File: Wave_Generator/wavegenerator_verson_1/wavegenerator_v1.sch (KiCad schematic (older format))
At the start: 56 parts, among them J1 01x06, J2 USB_B_Micro, J3 Conn_Coaxial, J6 1x2Pinheader, SW1 button, SW2 button, SW3 SP3T, U1 ATmega328P-AU, U3 LinReg, U4 MAX038CPP, U5 MC33063AD, U7 LM318N, Y1 16MHz

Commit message: OP AMP ERRORS
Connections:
- net GND: no longer U7.1 (BAL1), U7.5 (BAL3), U7.8 (BAL2)
- no-connect marks 3 -> 6
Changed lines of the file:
@@
 	0    -1   -1   0
-$EndComp
-$Comp
-L power:GND #PWR0103
-U 1 1 5D8C0155
-P 5500 1150
-F 0 "#PWR0103" H 5500 900 50  0001 C CNN
-F 1 "GND" H 5505 977 50  0000 C CNN
-F 2 "" H 5500 1150 50  0001 C CNN
-F 3 "" H 5500 1150 50  0001 C CNN
-	1    5500 1150
-	1    0    0    -1
 $EndComp
 Wire Wire Line
@@
 	-1   0    0    1
 $EndComp
-$Comp
-L power:GND #PWR0105
-U 1 1 5D8F5A55
-P 5450 1750
-F 0 "#PWR0105" H 5450 1500 50  0001 C CNN
-F 1 "GND" H 5550 1800 50  0000 C CNN
-F 2 "" H 5450 1750 50  0001 C CNN
-F 3 "" H 5450 1750 50  0001 C CNN
-	1    5450 1750
-	1    0    0    -1
-$EndComp
-Wire Wire Line
-	5350 1750 5450 1750
-Connection ~ 5450 1750
 Wire Wire Line
 	5650 1450 5650 1900
-Wire Wire Line
-	5350 1150 5500 1150
 Wire Wire Line
 	4350 1100 4350 1200
@@
 Wire Wire Line
 	1850 1200 2950 1200
+NoConn ~ 5350 1750
+NoConn ~ 5450 1750
+NoConn ~ 5350 1150
 $EndSCHEMATC

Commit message: wavegenerator changes
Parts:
- added TP5: WS_0, TestPoint:TestPoint_THTPad_2.5x2.5mm_Drill1.2mm, symbol Connector:TestPoint
- added TP6: WS_1, TestPoint:TestPoint_THTPad_2.5x2.5mm_Drill1.2mm, symbol Connector:TestPoint
- added TP7: Sync, TestPoint:TestPoint_THTPad_2.5x2.5mm_Drill1.2mm, symbol Connector:TestPoint
- added TP8: output, TestPoint:TestPoint_THTPad_2.5x2.5mm_Drill1.2mm, symbol Connector:TestPoint
- C4: renamed from C16; footprint Capacitor_THT:C_Disc_D3.0mm_W1.6mm_P2.50mm -> Capacitor_THT:C_Rect_L4.0mm_W2.5mm_P2.50mm
- C5: renamed from C17; footprint Capacitor_THT:C_Disc_D3.0mm_W1.6mm_P2.50mm -> Capacitor_THT:C_Rect_L4.0mm_W2.5mm_P2.50mm
- H1, H2, H3, H4: footprint MountingHole:MountingHole_2.1mm -> MountingHole:MountingHole_3.2mm_M3
- J1: value 01x06 -> 01x05; footprint wavegenerator_v1:01x06_pin_header -> wavegenerator_v1:01x05_pin_header
- R6: renamed from R11; value 1k -> 10k
- renumbered C13 to C1, C18 to C10, C1 to C101, C2 to C102, C14 to C103, C3 to C104, C4 to C105, C8 to C106, C11 to C107, C10 to C11, C15 to C2, C12 to C3, C5 to C6, C6 to C7, C7 to C8, R6 to R1, R8 to R101, R9 to R102, R10 to R103, R1 to R104, R5 to R2, R2 to R3, R3 to R4, R4 to R5, R12 to R7
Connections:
- net GND: now also J1.5
- net WS_0: now also TP5.1
- net WS_1: now also TP6.1
- net reset: now also J1.4, R104.2, SW2.1, U1.29 (~RESET~/PC6); no longer MOD1.5 (RES), U1.28 (PC5)
- net sync: now also U1.12 (PB0), TP7.1
- net switch_n: now reaches SW1.1, U1.2 (PD4)
- net MISO: now reaches J1.1, U1.16 (PB4)
- net output: now reaches RV3.3
- net output: now also TP8.1
- new net reset_lcd: MOD1.5 (RES), U1.28 (PC5)
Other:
- moved on the sheet: R104, SW1, SW2, TP1, TP2, TP3, TP4

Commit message: touch ups
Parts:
- added R8: 10k, Resistor_THT:R_Axial_DIN0207_L6.3mm_D2.5mm_P10.16mm_Horizontal, symbol Device:R_Small_US
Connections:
- net GND: now also U4.12 (PDO)
- net at U7.3 (+): now also R8.1; no longer RV3.2
- new net: R8.2, RV3.2
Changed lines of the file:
@@
 U 1 1 5D1B4472
 P 2500 5900
-F 0 "R103" H 2550 5950 50  0000 L CNN
-F 1 "10k" H 2550 5850 50  0000 L CNN
+F 0 "R103" H 2250 5950 50  0000 L CNN
+F 1 "10k" H 2300 5850 50  0000 L CNN
 F 2 "Resistor_SMD:R_0805_2012Metric" H 2500 5900 50  0001 C CNN
 F 3 "~" H 2500 5900 50  0001 C CNN
@@
 P 1500 6000
 F 0 "#PWR035" H 1500 5750 50  0001 C CNN
-F 1 "GND" H 1505 5827 50  0000 C CNN
+F 1 "GND" H 1500 5850 50  0000 C CNN
 F 2 "" H 1500 6000 50  0001 C CNN
 F 3 "" H 1500 6000 50  0001 C CNN
@@
 P 2500 6000
 F 0 "#PWR047" H 2500 5750 50  0001 C CNN
-F 1 "GND" H 2505 5827 50  0000 C CNN
+F 1 "GND" H 2500 5850 50  0000 C CNN
 F 2 "" H 2500 6000 50  0001 C CNN
 F 3 "" H 2500 6000 50  0001 C CNN
@@
 $EndComp
 Wire Wire Line
-	1050 5800 1350 5800
-Wire Wire Line
-	2700 5700 2700 6150
-Connection ~ 1350 5800
-Wire Wire Line
-	1350 5800 1500 5800
+	1050 5800 1150 5800
 Wire Wire Line
 	1250 4550 1250 4900
@@
 U 1 1 5D65F834
 P 4350 1350
-F 0 "RV3" H 4600 1550 50  0000 C CNN
-F 1 "10k" H 4600 1450 50  0000 C CNN
+F 0 "RV3" H 4500 1450 50  0000 C CNN
+F 1 "10k" H 4500 1550 50  0000 C CNN
 F 2 "wavegenerator_v1:Potentiometer_PTV09A" H 4350 1350 50  0001 C CNN
 F 3 "~" H 4350 1350 50  0001 C CNN
@@
 L power:-5V #PWR034
 U 1 1 5D4EAB46
-P 1350 6150
-F 0 "#PWR034" H 1350 6250 50  0001 C CNN
-F 1 "-5V" H 1365 6323 50  0000 C CNN
-F 2 "" H 1350 6150 50  0001 C CNN
-F 3 "" H 1350 6150 50  0001 C CNN
-	1    1350 6150
+P 1150 6200
+F 0 "#PWR034" H 1150 6300 50  0001 C CNN
+F 1 "-5V" H 1165 6373 50  0000 C CNN
+F 2 "" H 1150 6200 50  0001 C CNN
+F 3 "" H 1150 6200 50  0001 C CNN
+	1    1150 6200
 	-1   0    0    1
 $EndComp
-Connection ~ 1350 6150
 $Comp
 L power:GND #PWR08
@@
 L power:GND #PWR029
 U 1 1 5D370EFF
-P 2500 3300
-F 0 "#PWR029" H 2500 3050 50  0001 C CNN
-F 1 "GND" H 2505 3127 50  0000 C CNN
-F 2 "" H 2500 3300 50  0001 C CNN
-F 3 "" H 2500 3300 50  0001 C CNN
-	1    2500 3300
+P 2500 3250
+F 0 "#PWR029" H 2500 3000 50  0001 C CNN
+F 1 "GND" H 2505 3077 50  0000 C CNN
+F 2 "" H 2500 3250 50  0001 C CNN
+F 3 "" H 2500 3250 50  0001 C CNN
+	1    2500 3250
 	1    0    0    -1
 $EndComp
@@
 	1    0    0    -1
 $EndComp
-Wire Wire Line
-	1350 6150 1350 5800
 $Comp
 L Connector:TestPoint TP4
@@
 	1    0    0    -1
 $EndComp
-Wire Wire Line
-	1350 6150 2700 6150
 $Comp
 L power:-5V #PWR0108
@@
 	3100 5300 3100 5500
 Connection ~ 2700 5300
-Wire Wire Line
-	4500 1350 5050 1350
 $Comp
 L Connector:Conn_Coaxial J3
@@
 Text Label 9200 1100 0    50   ~ 0
 sync
+Connection ~ 1150 5800
+Wire Wire Line
+	1150 5800 1500 5800
+Wire Wire Line
+	2700 6200 1150 6200
+Wire Wire Line
+	2700 5700 2700 6200
+Wire Wire Line
+	1150 5800 1150 6200
+Connection ~ 1150 6200
+$Comp
+L Device:R_Small_US R8
+U 1 1 5D3AF030
+P 4750 1350
+F 0 "R8" V 4850 1400 50  0000 C CNN
+F 1 "10k" V 4950 1400 50  0000 C CNN
+F 2 "Resistor_THT:R_Axial_DIN0207_L6.3mm_D2.5mm_P10.16mm_Horizontal" H 4750 1350 50  0001 C CNN
+F 3 "~" H 4750 1350 50  0001 C CNN
+	1    4750 1350
+	0    1    1    0
+$EndComp
+Wire Wire Line
+	4500 1350 4650 1350
+Wire Wire Line
+	4850 1350 5050 1350
 $EndSCHEMATC

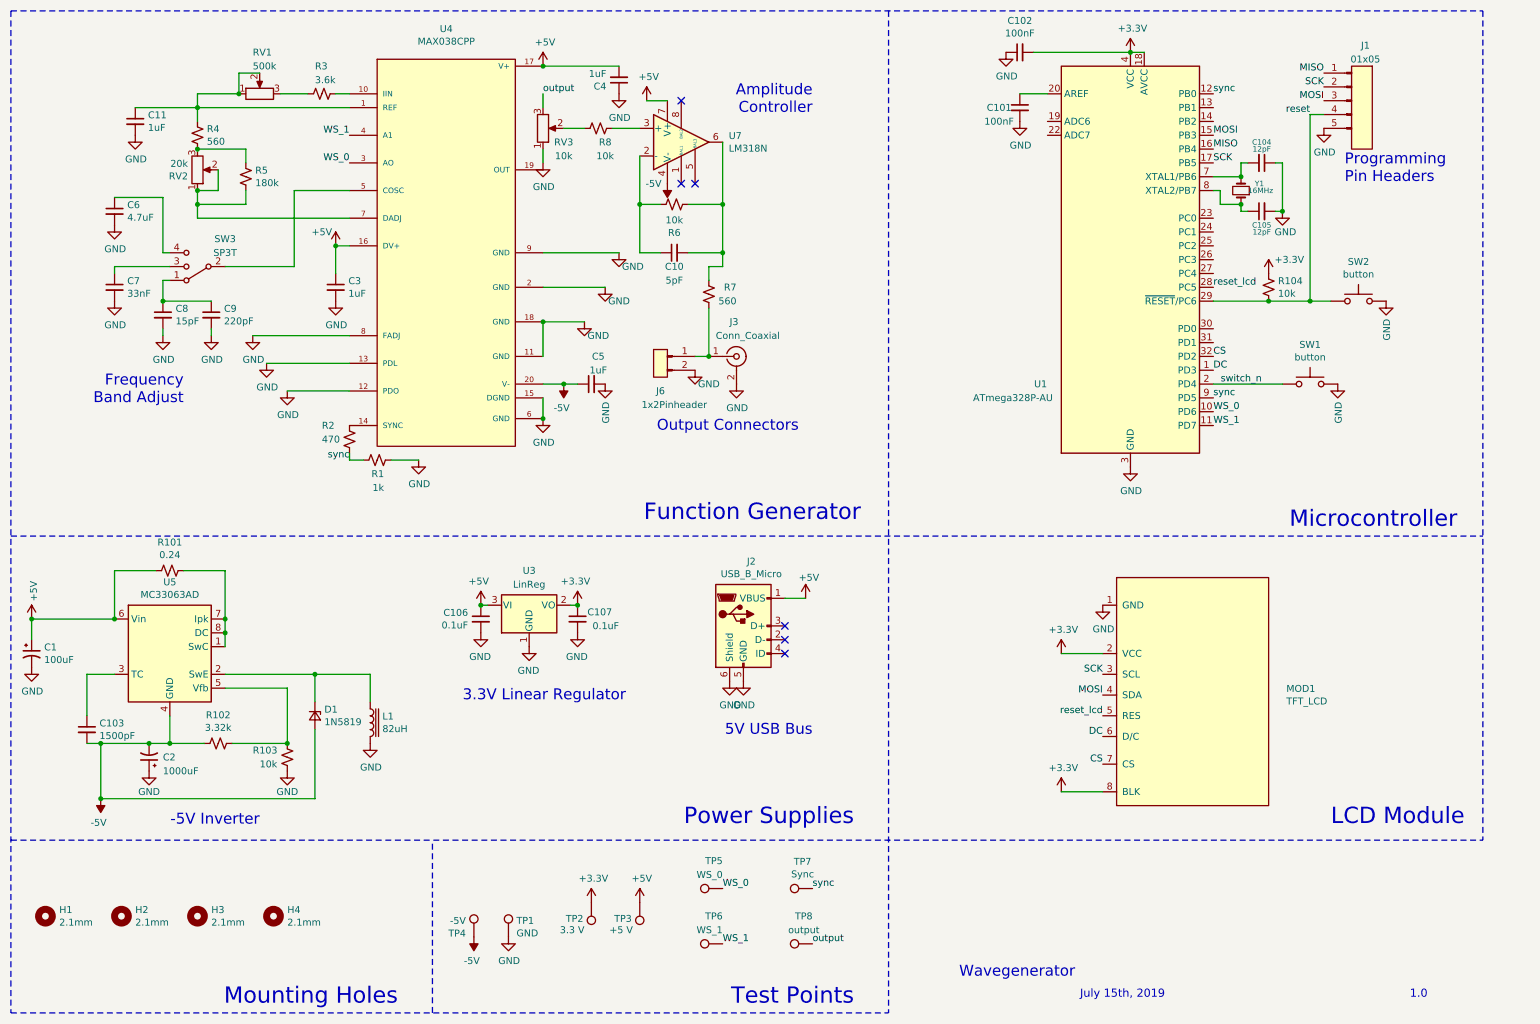
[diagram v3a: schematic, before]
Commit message: removed op amp and sync connection
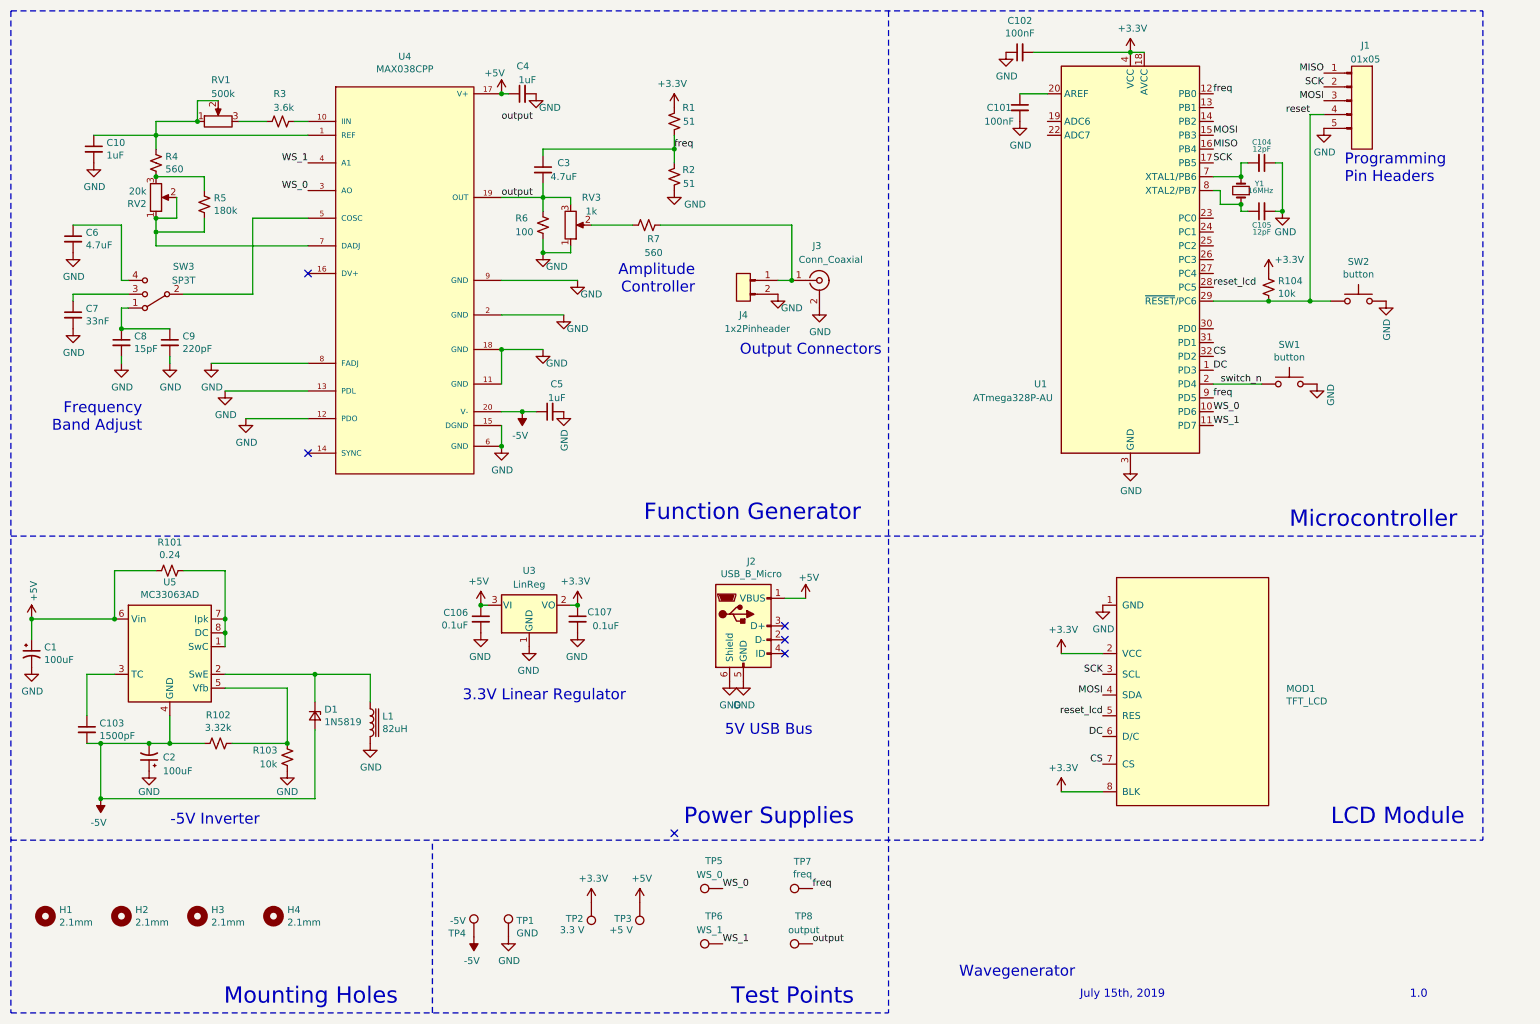
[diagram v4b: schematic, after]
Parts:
- removed C10: 5pF, Capacitor_THT:C_Rect_L4.0mm_W2.5mm_P2.50mm, symbol Device:C_Small
- removed R7: 560, Resistor_THT:R_Axial_DIN0207_L6.3mm_D2.5mm_P10.16mm_Horizontal, symbol Device:R_Small_US
- removed U7: LM318N, wavegenerator_v1:LM318N, symbol Amplifier_Operational:LM318N
- C2: value 1000uF -> 100uF
- C3: value 1uF -> 4.7uF
- R1: value 1k -> 51
- R2: value 470 -> 51
- R6: value 10k -> 100
- R7: renamed from R8; value 10k -> 560
- RV3: value 10k -> 1k
- TP7: value Sync -> freq
- renumbered C11 to C10, J6 to J4
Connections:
- net +3V3: now also R1.1
- net +5V: now also C4.1; no longer C3.1, C4.2, U4.16 (DV+)
- net GND: now also C4.2, R2.2, R6.2; no longer C3.2, C4.1, R1.2
- net output: now also C3.2, R6.1, U4.19 (OUT)
- net at U4.14 (SYNC): no longer R2.1
- net at R7.1: now also J3.1 (In), J4.1
- net sync renamed freq
- net freq: now also C3.1, R1.2, R2.1; no longer R1.1, R2.2
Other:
- moved on the sheet: C10, C4, C5, C6, C7, C8, C9, J3, J4, R3, R4, R5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

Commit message: naming
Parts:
- renumbered U3 to U1, U1 to U2, U5 to U3
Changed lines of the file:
@@
 	2050 5000 2050 5100
 $Comp
-L Regulator_Switching:MC33063AD U5
+L Regulator_Switching:MC33063AD U3
 U 1 1 5D1E6E42
 P 1650 5100
-F 0 "U5" H 1650 5567 50  0000 C CNN
+F 0 "U3" H 1650 5567 50  0000 C CNN
 F 1 "MC33063AD" H 1650 5476 50  0000 C CNN
 F 2 "Package_SO:SOIC-8_3.9x4.9mm_P1.27mm" H 1700 4650 50  0001 L CNN
@@
 	6100 4750 6250 4750
 $Comp
-L MCU_Microchip_ATmega:ATmega328P-AU U1
+L MCU_Microchip_ATmega:ATmega328P-AU U2
 U 1 1 5D258DD6
 P 8600 2300
-F 0 "U1" H 7950 1400 50  0000 C CNN
+F 0 "U2" H 7950 1400 50  0000 C CNN
 F 1 "ATmega328P-AU" H 7750 1300 50  0000 C CNN
 F 2 "Package_QFP:TQFP-32_7x7mm_P0.8mm" H 8600 2300 50  0001 C CIN
@@
 $EndComp
 $Comp
-L Regulator_Linear:AP1117-33 U3
+L Regulator_Linear:AP1117-33 U1
 U 1 1 5D2563E2
 P 4250 4800
-F 0 "U3" H 4250 5050 50  0000 C CNN
+F 0 "U1" H 4250 5050 50  0000 C CNN
 F 1 "LinReg" H 4250 4950 50  0000 C CNN
 F 2 "Package_TO_SOT_SMD:SOT-223-3_TabPin2" H 4250 4600 50  0001 C CIN

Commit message: numbering
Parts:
- added C5, C7: 10nF, Capacitor_THT:C_Rect_L4.0mm_W2.5mm_P2.50mm, symbol Device:C_Small
- renumbered C8 to C10, C9 to C11, C10 to C12, C5 to C6, C6 to C8, C7 to C9
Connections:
- net +5V: now also C5.2
- net -5V: now also C7.2
- net GND: now also C5.1, C7.1
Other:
- moved on the sheet: C6
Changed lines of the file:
@@
 $EndComp
 $Comp
-L Device:C_Small C8
+L Device:C_Small C10
 U 1 1 5D379378
 P 1300 2900
-F 0 "C8" H 1392 2946 50  0000 L CNN
+F 0 "C10" H 1392 2946 50  0000 L CNN
 F 1 "15pF" H 1392 2855 50  0000 L CNN
 F 2 "Capacitor_THT:C_Rect_L4.0mm_W2.5mm_P2.50mm" H 1300 2900 50  0001 C CNN
@@
 	1350 2650 1300 2650
 $Comp
-L Device:C_Small C6
+L Device:C_Small C8
 U 1 1 5D37A6B1
 P 950 2150
-F 0 "C6" H 1042 2196 50  0000 L CNN
+F 0 "C8" H 1042 2196 50  0000 L CNN
 F 1 "4.7uF" H 1042 2105 50  0000 L CNN
 F 2 "Capacitor_THT:C_Rect_L4.0mm_W2.5mm_P2.50mm" H 950 2150 50  0001 C CNN
@@
 $EndComp
 $Comp
-L Device:C_Small C7
+L Device:C_Small C9
 U 1 1 5D379EFA
 P 950 2700
-F 0 "C7" H 1042 2746 50  0000 L CNN
+F 0 "C9" H 1042 2746 50  0000 L CNN
 F 1 "33nF" H 1042 2655 50  0000 L CNN
 F 2 "Capacitor_THT:C_Rect_L4.0mm_W2.5mm_P2.50mm" H 950 2700 50  0001 C CNN
@@
 $EndComp
 $Comp
-L Device:C_Small C10
+L Device:C_Small C12
 U 1 1 5D2356A9
 P 1100 1500
-F 0 "C10" H 1192 1546 50  0000 L CNN
+F 0 "C12" H 1192 1546 50  0000 L CNN
 F 1 "1uF" H 1192 1455 50  0000 L CNN
 F 2 "Capacitor_THT:C_Rect_L4.0mm_W2.5mm_P2.50mm" H 1100 1500 50  0001 C CNN
@@
 $EndComp
 $Comp
-L Device:C_Small C5
+L Device:C_Small C6
 U 1 1 5D248DFE
-P 4400 3400
-F 0 "C5" V 4600 3350 50  0000 C CNN
-F 1 "1uF" V 4500 3350 50  0000 C CNN
-F 2 "Capacitor_THT:C_Rect_L4.0mm_W2.5mm_P2.50mm" H 4400 3400 50  0001 C CNN
-F 3 "~" H 4400 3400 50  0001 C CNN
-	1    4400 3400
+P 4450 3400
+F 0 "C6" V 4650 3400 50  0000 C CNN
+F 1 "1uF" V 4550 3400 50  0000 C CNN
+F 2 "Capacitor_THT:C_Rect_L4.0mm_W2.5mm_P2.50mm" H 4450 3400 50  0001 C CNN
+F 3 "~" H 4450 3400 50  0001 C CNN
+	1    4450 3400
 	0    -1   -1   0
 $EndComp
@@
 L power:GND #PWR045
 U 1 1 5D24B84C
-P 4500 3400
-F 0 "#PWR045" H 4500 3150 50  0001 C CNN
-F 1 "GND" V 4505 3272 50  0000 R CNN
-F 2 "" H 4500 3400 50  0001 C CNN
-F 3 "" H 4500 3400 50  0001 C CNN
-	1    4500 3400
+P 4650 3600
+F 0 "#PWR045" H 4650 3350 50  0001 C CNN
+F 1 "GND" H 4850 3500 50  0000 R CNN
+F 2 "" H 4650 3600 50  0001 C CNN
+F 3 "" H 4650 3600 50  0001 C CNN
+	1    4650 3600
 	1    0    0    -1
 $EndComp
@@
 	-1   0    0    1
 $EndComp
-Wire Wire Line
-	4200 3400 4300 3400
 $Comp
 L power:-5V #PWR034
@@
 L power:GND #PWR042
 U 1 1 5D298258
-P 4300 1100
-F 0 "#PWR042" H 4300 850 50  0001 C CNN
-F 1 "GND" H 4400 1000 50  0000 C CNN
-F 2 "" H 4300 1100 50  0001 C CNN
-F 3 "" H 4300 1100 50  0001 C CNN
-	1    4300 1100
+P 4400 1350
+F 0 "#PWR042" H 4400 1100 50  0001 C CNN
+F 1 "GND" H 4500 1250 50  0000 C CNN
+F 2 "" H 4400 1350 50  0001 C CNN
+F 3 "" H 4400 1350 50  0001 C CNN
+	1    4400 1350
 	1    0    0    -1
 $EndComp
@@
 $EndComp
 $Comp
-L Device:C_Small C9
+L Device:C_Small C11
 U 1 1 5D573068
 P 1650 2900
-F 0 "C9" H 1742 2946 50  0000 L CNN
+F 0 "C11" H 1742 2946 50  0000 L CNN
 F 1 "220pF" H 1742 2855 50  0000 L CNN
 F 2 "Capacitor_THT:C_Rect_L4.0mm_W2.5mm_P2.50mm" H 1650 2900 50  0001 C CNN
@@
 Text Label 6300 6850 0    50   ~ 0
 freq
-Text Label 4050 1300 0    50   ~ 0
-output
 Text Label 6300 7250 0    50   ~ 0
 output
@@
 Wire Wire Line
 	4700 2050 5000 2050
+$Comp
+L Device:C_Small C5
+U 1 1 5D571033
+P 4200 1300
+F 0 "C5" V 4300 1300 50  0000 C CNN
+F 1 "10nF" V 4400 1300 50  0000 C CNN
+F 2 "Capacitor_THT:C_Rect_L4.0mm_W2.5mm_P2.50mm" H 4200 1300 50  0001 C CNN
+F 3 "~" H 4200 1300 50  0001 C CNN
+	1    4200 1300
+	0    1    1    0
+$EndComp
+Wire Wire Line
+	4050 1100 4050 1300
+Wire Wire Line
+	4050 1300 4100 1300
+Wire Wire Line
+	4300 1300 4400 1300
+Wire Wire Line
+	4400 1300 4400 1100
+Wire Wire Line
+	4400 1100 4300 1100
+Connection ~ 4400 1300
+Wire Wire Line
+	4400 1300 4400 1350
+$Comp
+L Device:C_Small C7
+U 1 1 5D5888D6
+P 4450 3600
+F 0 "C7" V 4550 3600 50  0000 C CNN
+F 1 "10nF" V 4650 3600 50  0000 C CNN
+F 2 "Capacitor_THT:C_Rect_L4.0mm_W2.5mm_P2.50mm" H 4450 3600 50  0001 C CNN
+F 3 "~" H 4450 3600 50  0001 C CNN
+	1    4450 3600
+	0    1    1    0
+$EndComp
+Wire Wire Line
+	4200 3400 4350 3400
+Wire Wire Line
+	4350 3400 4350 3600
+Connection ~ 4350 3400
+Wire Wire Line
+	4550 3600 4650 3600
+Wire Wire Line
+	4550 3400 4650 3400
+Wire Wire Line
+	4650 3400 4650 3600
+Connection ~ 4650 3600
 $EndSCHEMATC
